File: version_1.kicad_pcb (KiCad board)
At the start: 2 copper layers, 98.6 x 99.9 mm, 135 parts, among them J1 motor_connector, J2 motor_connector, J3 motor_connector, J4 motor_connector, M5 Motor_Servo_JR, M6 Motor_Servo_JR, M7 Motor_Servo_JR, M8 Motor_Servo_JR, Q1 AO3400A, Q10 AO3400A, Q11 AO3400A, Q12 AO3400A, Q13 AO3400A, Q14 AO3400A, Q15 AO3400A, Q16 AO3400A, Q17 AO3401A, Q18 AO3401A, Q19 AO3401A, Q2 AO3400A, Q20 AO3401A, Q21 AO3400A, Q22 AO3400A, Q23 AO3400A, Q24 AO3400A, Q25 AO3400A, Q3 AO3400A, Q4 AO3400A, Q5 AO3400A, Q6 AO3400A, Q7 AO3400A, Q8 AO3400A, Q9 AO3400A, SW1 SW_SPDT, U1 Pico, U10 74AHC595, U11 ADP2302ARDZ-5.0, U12 LSM6DS3, U2 SLM2009, U3 SLM2009, U4 SLM2009, U5 SLM2009, U6 SLM2009, U7 SLM2009, U8 SLM2009, U9 SLM2009

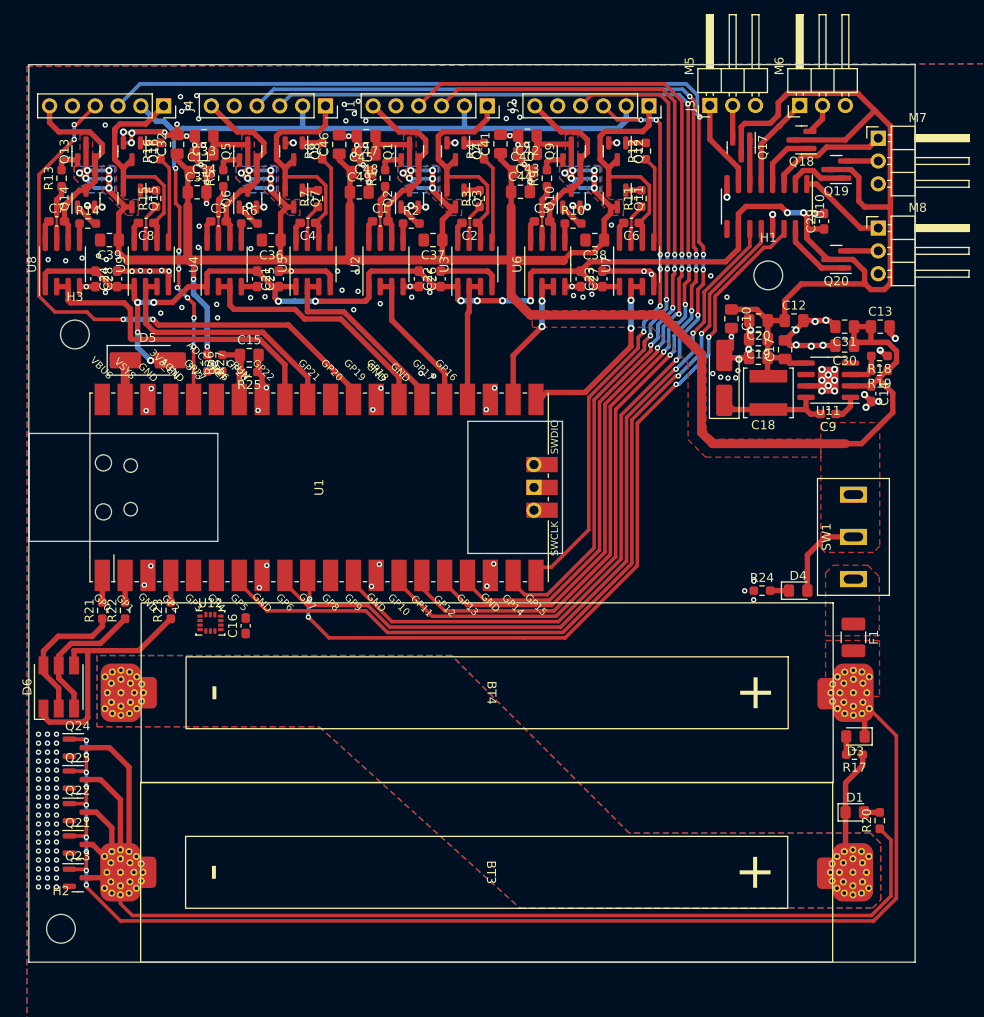
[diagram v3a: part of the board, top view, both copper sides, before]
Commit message: version 1.1 item colisions fixed added silkscreen DRC done
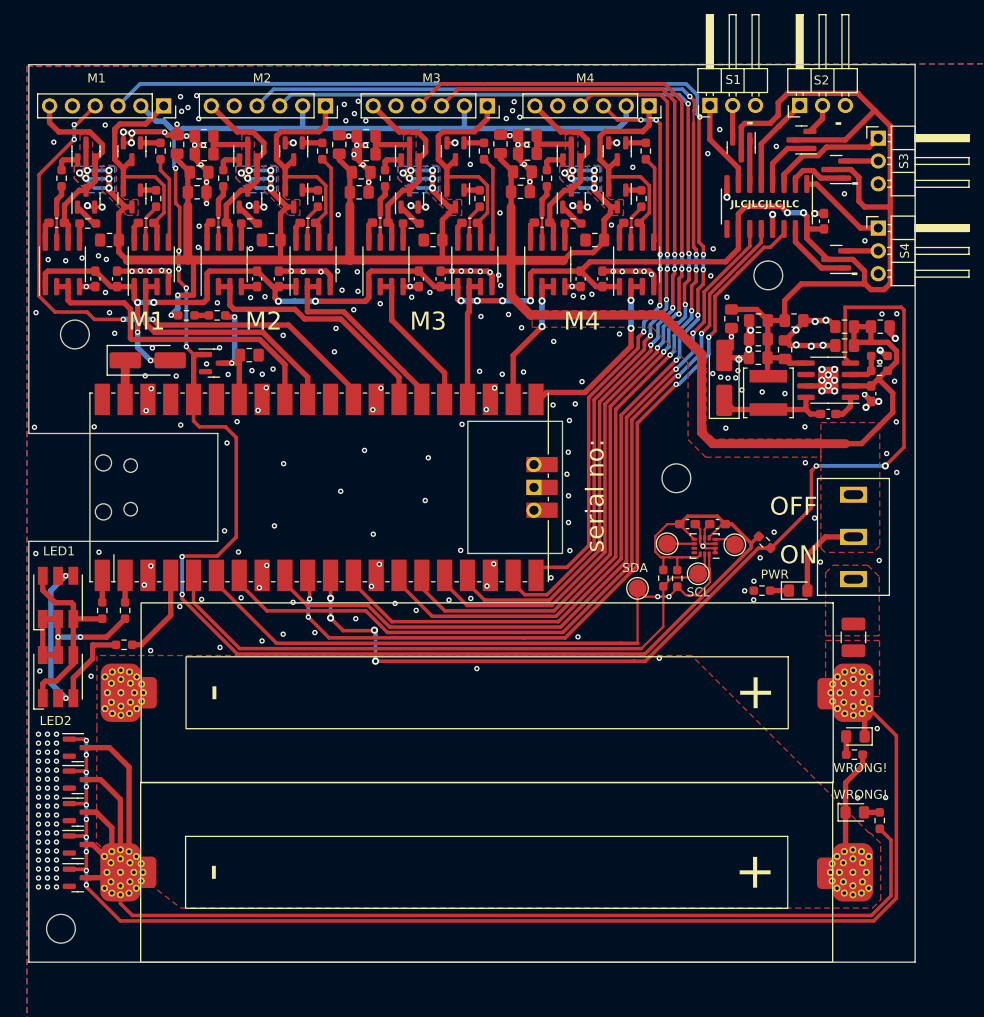
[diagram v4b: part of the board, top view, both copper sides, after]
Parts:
- removed R25: 1k, Resistor_SMD:R_0603_1608Metric_Pad0.98x0.95mm_HandSolder
- added C50: 100n, Capacitor_SMD:C_0603_1608Metric_Pad1.08x0.95mm_HandSolder, F.Cu at (100.2, 72.5)
- added D7: C2843868, LED_SMD:LED_RGB_5050-6, F.Cu at (26.9, 80.7)
- added H4: MountingHole, MountingHole:MountingHole_3.2mm_M3, F.Cu at (95.7, 67.4)
- added Q26: AO3400A, Package_TO_SOT_SMD:SOT-23, F.Cu at (44.2, 54.6)
- added R28: 1k, Resistor_SMD:R_0603_1608Metric_Pad0.98x0.95mm_HandSolder, F.Cu at (105.5, 74.5)
- added R29: 1k, Resistor_SMD:R_0603_1608Metric_Pad0.98x0.95mm_HandSolder, F.Cu at (95.8, 78.6)
- added R30: 1k, Resistor_SMD:R_0603_1608Metric_Pad0.98x0.95mm_HandSolder, F.Cu at (94.2, 78.5)
- added TP1: TestPoint, TestPoint:TestPoint_Pad_D2.0mm, F.Cu at (102.2, 74.8)
- added TP2: TestPoint, TestPoint:TestPoint_Pad_D2.0mm, F.Cu at (94.7, 74.7)
- added TP3: SDA, TestPoint:TestPoint_Pad_D2.0mm, F.Cu at (91.3, 79.7)
- added TP4: SCL, TestPoint:TestPoint_Pad_D2.0mm, F.Cu at (98.1, 78.0)
- moved U12 55.7 mm to (98.8, 75.0), turned to 180 degrees
- moved C16 50.4 mm to (96.9, 72.5), turned to 0 degrees
- moved R23 6.44 mm to (34.2, 86.0), turned to 0 degrees
- moved R27 5.80 mm to (41.1, 49.3), turned to 0 degrees
- moved R26 5.34 mm to (44.6, 49.3), turned to 0 degrees
- moved D6 1.15 mm to (26.9, 89.5)
- moved C7 0.16 mm to (26.7, 39.0)
- moved C1 0.13 mm to (62.7, 39.0)
- moved C3 0.13 mm to (44.7, 39.0)
- moved C5 0.13 mm to (80.7, 39.0)
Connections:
- C16 pad 1: +5V -> +3.3V
- D6 pad 2: Net-(D6-GK) -> Net-(D6-BK)
- D6 pad 5: Net-(D6-BK) -> Net-(D6-GA)
- D6 pad 6: Net-(D6-GK) -> Net-(D6-GA)
- R21 pad 1: Net-(D6-GK) -> Net-(D6-BA)
- R22 pad 1: Net-(D6-BK) -> Net-(D6-GA)
- R23 pad 1: Net-(D6-BA) -> Net-(D6-BK)
- U1 pad 11: unconnected-(U1-GPIO8-Pad11) -> /power/Pgood
- U1 pad 5: unconnected-(U1-GPIO3-Pad5) -> /SCL
- U1 pad 6: unconnected-(U1-GPIO4-Pad6) -> /SDA
- U12 pad 1: unconnected-(U12-SDO/SA0-Pad1) -> GND
- U12 pad 12: unconnected-(U12-CS-Pad12) -> +3.3V
- U12 pad 13: unconnected-(U12-SCL-Pad13) -> /SCL
- U12 pad 14: unconnected-(U12-SDA-Pad14) -> /SDA
- U12 pad 2: unconnected-(U12-SDX-Pad2) -> GND
- U12 pad 3: unconnected-(U12-SCX-Pad3) -> GND
- U12 pad 4: unconnected-(U12-INT1-Pad4) -> Net-(U12-INT1)
- U12 pad 5: unconnected-(U12-VDDIO-Pad5) -> +3.3V
- U12 pad 6: Net-(U12-GND-Pad6) -> GND
- U12 pad 7: Net-(U12-GND-Pad6) -> GND
- U12 pad 8: unconnected-(U12-VDD-Pad8) -> +3.3V
- U12 pad 9: unconnected-(U12-INT2-Pad9) -> Net-(U12-INT2)
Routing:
- net +3.3V: track 94.3 -> 225.4 mm
- net /power/Pgood: track 0.00 -> 114.8 mm, vias 0 -> 6
- net /SDA: track 0.00 -> 70.8 mm, vias 0 -> 2
- net /SCL: track 0.00 -> 70.7 mm
- net Net-(D6-GA): track 0.00 -> 19.8 mm, vias 0 -> 2
- net Net-(D6-GK): track 15.6 -> 0.00 mm
- net Net-(D6-BK): track 15.7 -> 27.8 mm, vias 0 -> 2
- net Net-(U1-GPIO2): track 3.89 -> 11.0 mm
- net Net-(Q26-D): track 7.93 -> 14.2 mm, vias 0 -> 2
- net Net-(D6-BA): track 27.6 -> 21.4 mm
- net GND: track 133.5 -> 138.8 mm, vias 195 -> 305
- net VCC: track 412.0 -> 409.0 mm
- net Net-(U12-INT2): track 0.00 -> 3.01 mm
- net Net-(U12-INT1): track 0.00 -> 2.44 mm
- net /ENCODER6: track 63.2 -> 64.2 mm
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- removed copper zone on B.Cu, net Net-(BT3-+)
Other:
- board text added: "-"
- board text added: "JLCJLCJLCJLC"
- board text added: "LED1"
- board text added: "LED2"
- board text added: "OFF"
- board text added: "ON"
- board text added: "S1"
- board text added: "S2"
- board text added: "S3"
- board text added: "S4"
- board text added: "designed by: Michał Pietrzak"
- board text added: "for: Fundacja Adamed www.fundacjaadamed.pl"
- board text added: "serial no:"
